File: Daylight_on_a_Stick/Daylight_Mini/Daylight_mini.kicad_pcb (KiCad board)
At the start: 2 copper layers, 170 x 11 mm, 24 parts, among them J1 Conn_01x02, J2 Conn_01x02

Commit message: Fixed some Layout LED footprint issues
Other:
- board text added: "Daylight on a stick by Blamm Daybreak Mini by Vector 3D V2.1"
- board text removed: "Daylight on a stick by Blamm Daybreak Mini by Vector 3D V2"
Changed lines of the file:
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@@
     (effects (font (size 1.5 1.5) (thickness 0.25)) (justify right mirror))
   )
-  (gr_text "Daylight on a stick by Blamm\nDaybreak Mini by Vector 3D\nV2" (at 98 33) (layer "B.SilkS")
+  (gr_text "Daylight on a stick by Blamm\nDaybreak Mini by Vector 3D\nV2.1" (at 98 33) (layer "B.SilkS")
     (effects (font (size 1 1) (thickness 0.15)) (justify mirror))
   )
@@
     (connect_pads (clearance 0.508))
     (min_thickness 0.254) (filled_areas_thickness no)
-    (fill yes (thermal_gap 0.508) (thermal_bridge_width 0.508))
+    (fill yes (thermal_gap 0.5) (thermal_bridge_width 0.5))
     (polygon
       (pts
@@
     (connect_pads (clearance 0.508))
     (min_thickness 0.254) (filled_areas_thickness no)
-    (fill yes (thermal_gap 0) (thermal_bridge_width 0.508))
+    (fill yes (thermal_gap 0.5) (thermal_bridge_width 0.5))
     (polygon
       (pts
@@
     (connect_pads (clearance 0.508))
     (min_thickness 0.254) (filled_areas_thickness no)
-    (fill yes (thermal_gap 0.508) (thermal_bridge_width 0.8))
+    (fill yes (thermal_gap 0.5) (thermal_bridge_width 0.5))
     (polygon
       (pts

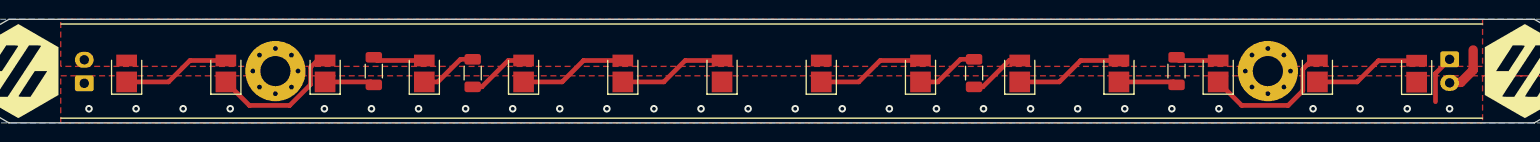
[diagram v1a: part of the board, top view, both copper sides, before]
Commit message: Daylight (all) V2.2
The JST XH silkscreen did not match the connectors very well so it has been adjusted.
Added small front silkscreen to indicate pins
Adjusted one connector on day_mini that was misplaced 1mm.
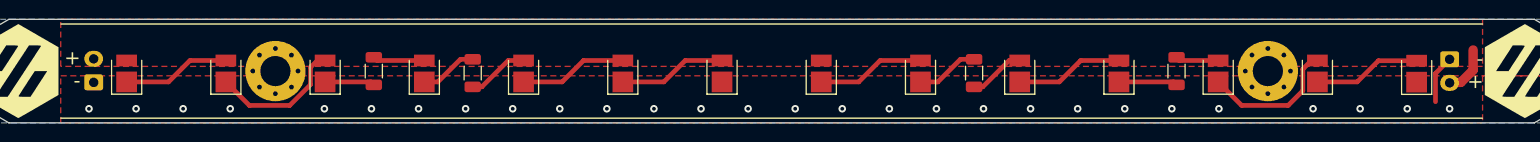
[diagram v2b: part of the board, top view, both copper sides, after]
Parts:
- J1, J2: footprint Connector_JST:JST_XH_S2B-XH-A_1x02_P2.50mm_Horizontal -> Daylight:JST_XH_S2B-XH-A_1x02_P2.50mm_Horizontal Daylight
- moved J1 1.00 mm to (26.0, 34.2)
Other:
- board text added: "+ -"
- board text added: "- +"
- board text added: "Daylight on a stick by Blamm Daybreak Mini by Vector 3D V2.2"
- board text removed: "Daylight on a stick by Blamm Daybreak Mini by Vector 3D V2.1"
